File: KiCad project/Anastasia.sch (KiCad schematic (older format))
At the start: 2 parts

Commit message: Refactoring
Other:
- moved on the sheet: TP7
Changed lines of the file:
@@
 LIBS:memory
 LIBS:xilinx
-LIBS:special
 LIBS:microcontrollers
 LIBS:dsp
@@
 Connection ~ 7900 1900
 Wire Wire Line
-	7750 2700 8150 2700
-Connection ~ 7750 2100
+	7800 2700 8150 2700
+Connection ~ 7800 2100
 Wire Wire Line
 	4200 2850 4650 2850
@@
 L TESTPAD TP7
 U 1 1 550D3AEA
-P 7600 2350
-F 0 "TP7" H 7850 2350 60  0000 C CNN
-F 1 "TESTPAD" H 7650 2150 60  0001 C CNN
-F 2 "Anastasia:Test_Point_Round-SMD-Pad" H 7850 2350 60  0001 C CNN
-F 3 "" H 7850 2350 60  0000 C CNN
-	1    7600 2350
+P 7650 2350
+F 0 "TP7" H 7900 2350 60  0000 C CNN
+F 1 "TESTPAD" H 7700 2150 60  0001 C CNN
+F 2 "Anastasia:Test_Point_Round-SMD-Pad" H 7900 2350 60  0001 C CNN
+F 3 "" H 7900 2350 60  0000 C CNN
+	1    7650 2350
 	0    1    1    0
 $EndComp
 Wire Wire Line
-	7600 2350 7600 2000
-Connection ~ 7600 2000
+	7650 2350 7650 2000
+Connection ~ 7650 2000
 Wire Wire Line
 	2900 4100 2650 4100
@@
 	8150 1650 7550 1650
 Wire Wire Line
-	8150 1450 7950 1450
-Wire Wire Line
-	7950 1450 7950 850
-Wire Wire Line
-	7950 850  9700 850
+	8150 1450 8050 1450
+Wire Wire Line
+	8050 1450 8050 850
+Wire Wire Line
+	8050 850  9700 850
 Wire Wire Line
 	9700 850  9700 4100
@@
 	6350 2150 6400 2150
 Wire Wire Line
-	6400 2000 6150 2000
-Wire Wire Line
-	6150 2000 6150 3450
-Wire Wire Line
-	6150 3450 8150 3450
+	6400 2000 6250 2000
+Wire Wire Line
+	6250 2000 6250 3450
+Wire Wire Line
+	6250 3450 8150 3450
 Wire Wire Line
 	4200 4250 4450 4250
@@
 	6000 4700 4200 4700
 Wire Wire Line
-	4200 4850 6050 4850
-Wire Wire Line
-	6050 4850 6050 1850
-Wire Wire Line
-	6050 1850 5900 1850
-Wire Wire Line
-	7750 2100 7750 2700
+	4200 4850 6100 4850
+Wire Wire Line
+	6100 4850 6100 1850
+Wire Wire Line
+	6100 1850 5900 1850
+Wire Wire Line
+	7800 2100 7800 2700
 Wire Wire Line
 	4150 2150 4250 2150

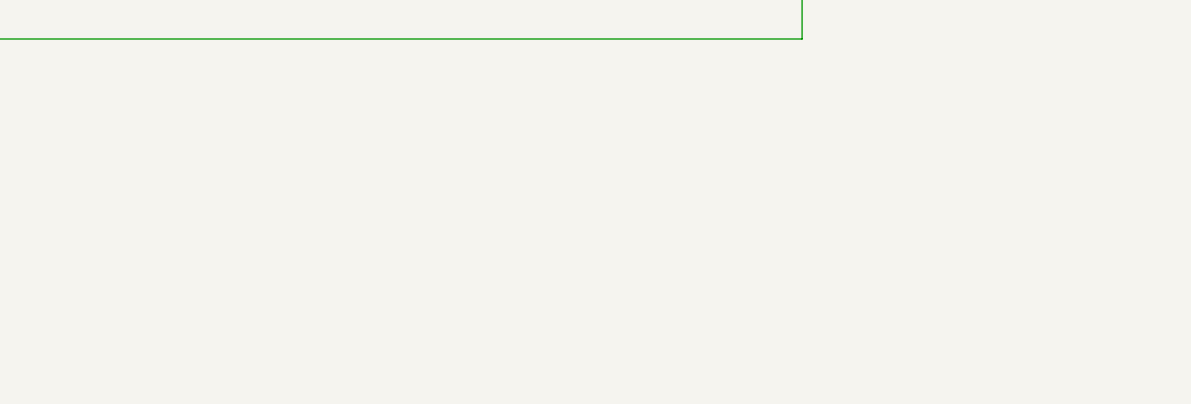
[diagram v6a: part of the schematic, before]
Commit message: Modifications for compliance with CERN OHL
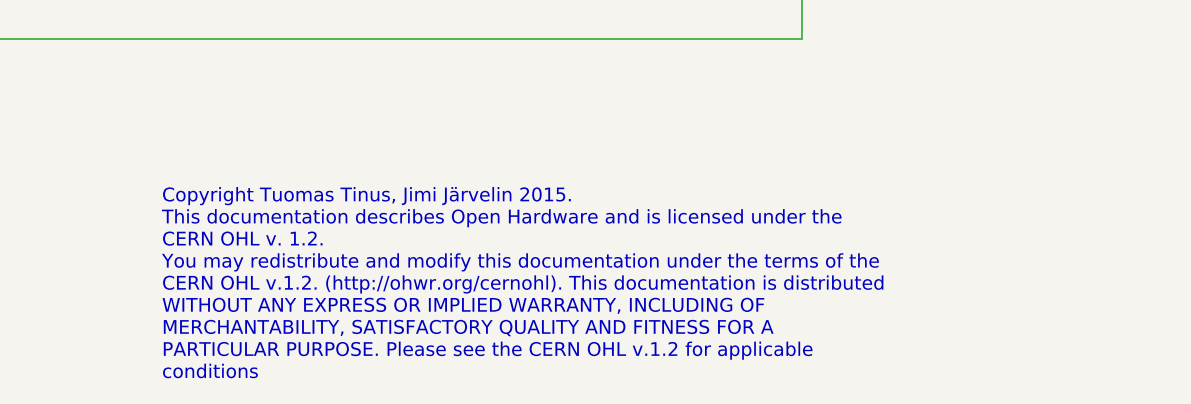
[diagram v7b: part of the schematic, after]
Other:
- note added: "Copyright Tuomas Tinus, Jimi Järvelin 2015.\nThis documentation describes Open Hardware and is licensed under the\nCERN OHL v. 1.2.\nYou may redistribute and modify this documentation under the terms of the\nCERN OHL v.1.2. (http://ohwr.org/cernohl). This documentation is distributed\nWITHOUT ANY EXPRESS OR IMPLIED WARRANTY, INCLUDING OF\nMERCHANTABILITY, SATISFACTORY QUALITY AND FITNESS FOR A\nP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"
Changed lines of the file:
@@
 	4350 2050 4350 2850
 Connection ~ 4350 2850
+Text Notes 6900 5600 0    60   ~ 0
+Copyright Tuomas Tinus, Jimi Järvelin 2015.\nThis documentation describes Open Hardware and is licensed under the\nCERN OHL v. 1.2.\nYou may redistribute and modify this documentation under the terms of the\nCERN OHL v.1.2. (http://ohwr.org/cernohl). This documentation is distributed\nWITHOUT ANY EXPRESS OR IMPLIED WARRANTY, INCLUDING OF\nMERCHANTABILITY, SATISFACTORY QUALITY AND FITNESS FOR A\nPARTICULAR PURPOSE. Please see the CERN OHL v.1.2 for applicable\nconditions
 $EndSCHEMATC
